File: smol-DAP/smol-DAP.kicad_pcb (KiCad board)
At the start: 4 copper layers, 32.5 x 13.4 mm, 30 parts, among them J1 USB_C_Receptacle_USB2.0, J2 Conn_ARM_JTAG_SWD_10, J3 Conn_02x05_Odd_Even, U1 AP2127K-3.3, U2 STM32F103CBTx, Y1 8MHz

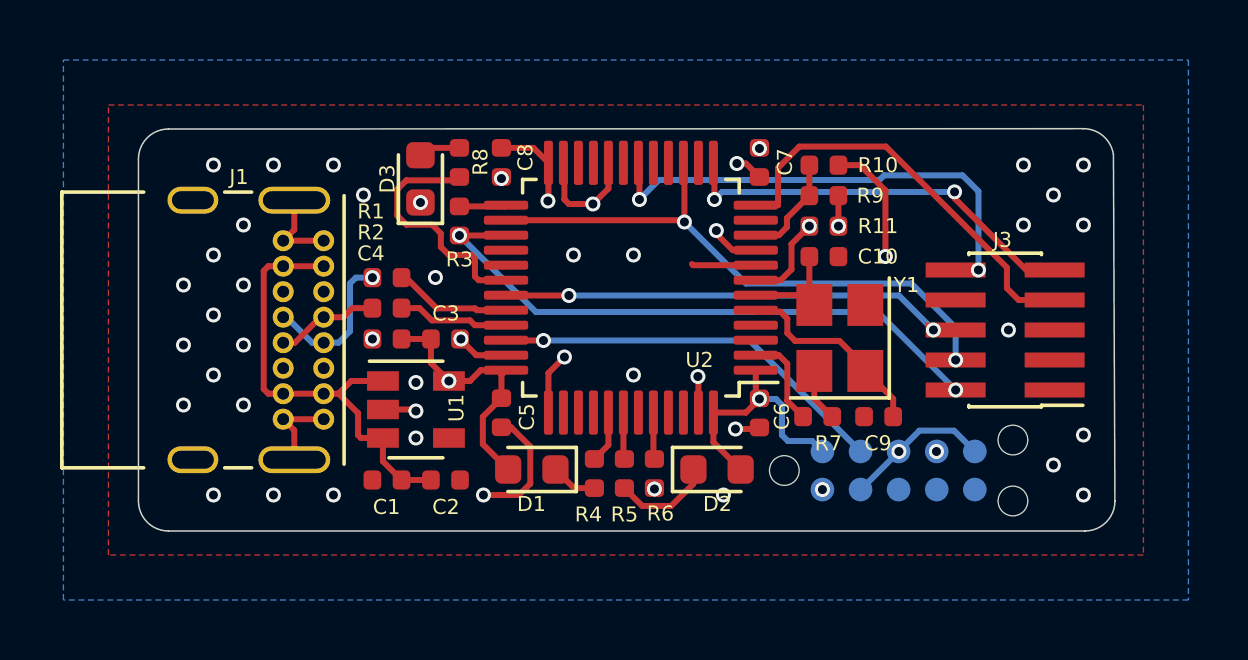
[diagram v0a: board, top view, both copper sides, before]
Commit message: Down to two layers
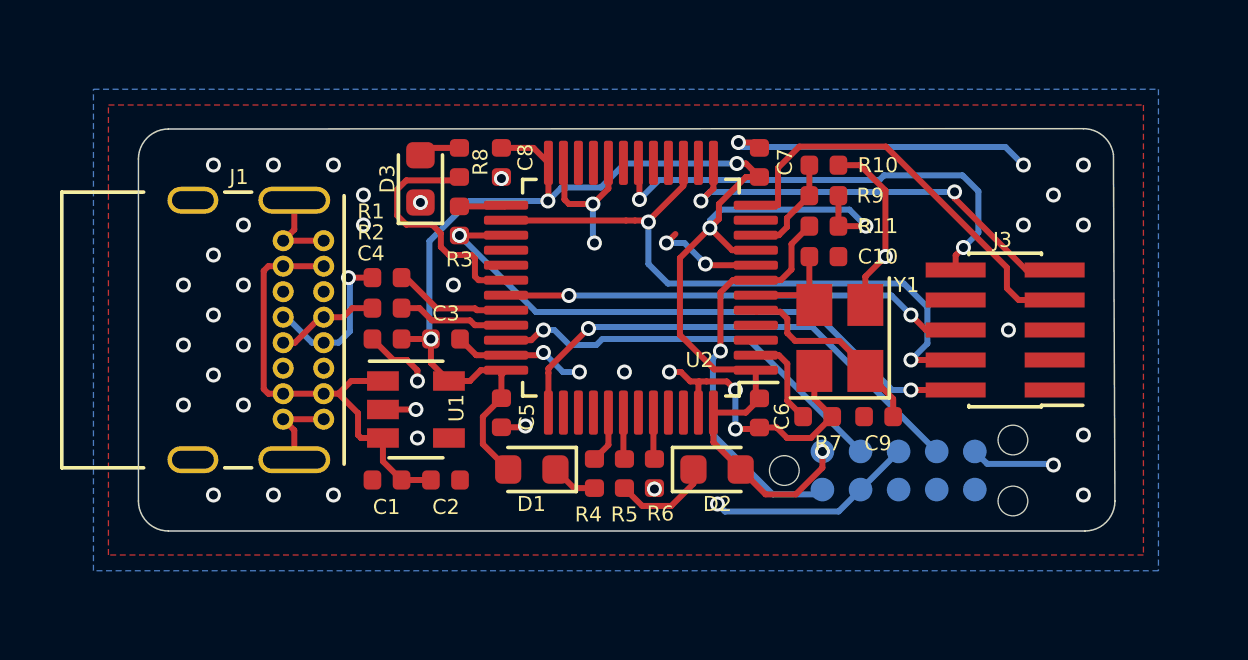
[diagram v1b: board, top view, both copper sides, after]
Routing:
- net GND: track 31.6 -> 60.3 mm, vias 46 -> 48
- net +3V3: track 51.3 -> 55.7 mm
- net TGT_SWCLK: track 19.5 -> 22.0 mm
- net ~RESET: track 12.0 -> 13.8 mm, vias 2 -> 1
- net SWCLK: track 15.8 -> 16.7 mm, vias 2 -> 1
- net TGT_SWO: track 15.5 -> 16.2 mm
- net TGT_TX: track 13.9 -> 14.6 mm
- removed copper zone on In1.Cu, net GND
- removed copper zone on In2.Cu, net GND
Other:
- copper layers 4 -> 2
- board text added: "smol"
